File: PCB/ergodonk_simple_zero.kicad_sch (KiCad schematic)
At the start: 147 parts, among them J2 4PIN, Q1 TIP120, SW0 SW_PUSH_LED, SW08 SW_PUSH_LED, SW1 SW_PUSH_LED, SW10 SW_PUSH_LED, SW11 SW_PUSH_LED, SW12 SW_PUSH_LED, SW13 SW_PUSH_LED, SW14 SW_PUSH_LED, SW15 SW_PUSH_LED, SW16 SW_PUSH_LED, SW17 SW_PUSH_LED, SW18 SW_PUSH_LED, SW2 SW_PUSH_LED, SW20 SW_PUSH_LED, SW21 SW_PUSH_LED, SW22 SW_PUSH_LED, SW23 SW_PUSH_LED, SW24 SW_PUSH_LED, SW25 SW_PUSH_LED, SW26 SW_PUSH_LED, SW27 SW_PUSH_LED, SW28 SW_PUSH_LED, SW3 SW_PUSH_LED, SW30 SW_PUSH_LED, SW31 SW_PUSH_LED, SW32 SW_PUSH_LED, SW33 SW_PUSH_LED, SW34 SW_PUSH_LED, SW35 SW_PUSH_LED, SW36 SW_PUSH_LED, SW37 SW_PUSH_LED, SW38 SW_PUSH_LED, SW4 SW_PUSH_LED, SW40 SW_PUSH_LED, SW42 SW_PUSH_LED, SW43 SW_PUSH_LED, SW44 SW_PUSH_LED, SW45 SW_PUSH_LED, SW46 SW_PUSH_LED, SW47 SW_PUSH_LED, SW48 SW_PUSH_LED, SW5 SW_PUSH_LED, SW50 SW_PUSH_LED, SW51 SW_PUSH_LED, SW52 SW_PUSH_LED, SW53 SW_PUSH_LED, SW54 SW_PUSH_LED, SW55 SW_PUSH_LED, SW56 SW_PUSH_LED, SW57 SW_PUSH_LED, SW58 SW_PUSH_LED, SW6 SW_PUSH_LED, SW7 SW_PUSH_LED

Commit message: Fixed key plate hole width bug Updated home position for keyplate footprints Generated bottom plate for acrylic production
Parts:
- H20, H24, H4: footprint Ergodonk_simple_zero:Hole from sofle for M2 posts gold rimmer -> Ergodonk_simple_zero:M2 Standoff hole - keyplate passthrough
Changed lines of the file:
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@@
       (effects (font (size 1.27 1.27)) (justify left))
     )
-    (property "Footprint" "Ergodonk_simple_zero:Hole from sofle for M2 posts gold rimmer" (at 273.05 229.87 0)
+    (property "Footprint" "Ergodonk_simple_zero:M2 Standoff hole - keyplate passthrough" (at 273.05 229.87 0)
       (effects (font (size 1.27 1.27)) hide)
     )
@@
       (effects (font (size 1.27 1.27)) (justify left))
     )
-    (property "Footprint" "Ergodonk_simple_zero:Hole from sofle for M2 posts gold rimmer" (at 223.52 229.87 0)
+    (property "Footprint" "Ergodonk_simple_zero:M2 Standoff hole - keyplate passthrough" (at 223.52 229.87 0)
       (effects (font (size 1.27 1.27)) hide)
     )
@@
       (effects (font (size 1.27 1.27)) (justify left))
     )
-    (property "Footprint" "Ergodonk_simple_zero:Hole from sofle for M2 posts gold rimmer" (at 251.46 260.35 0)
-      (effects (font (size 1.27 1.27)) hide)
-    )
+    (property "Footprint" "Ergodonk_simple_zero:M2 Standoff hole - keyplate passthrough" (at 251.46 260.35 0)
+      (effects (font (size 1.27 1.27)) hide)
+    )

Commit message: Fixed switched thumb keys for SA labels
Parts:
- SW51: LH + -> 0
- SW52: LH 0 -> +
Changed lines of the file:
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@@
       (effects (font (size 1.27 1.27)) hide)
     )
-    (property "LH" "0" (at 364.49 149.86 0) (show_name)
+    (property "LH" "+" (at 364.49 149.86 0) (show_name)
       (effects (font (size 1.27 1.27)))
     )
@@
       (effects (font (size 1.27 1.27)) hide)
     )
-    (property "LH" "+" (at 386.08 149.86 0) (show_name)
-      (effects (font (size 1.27 1.27)))
-    )
+    (property "LH" "0" (at 386.08 149.86 0) (show_name)
+      (effects (font (size 1.27 1.27)))
+    )

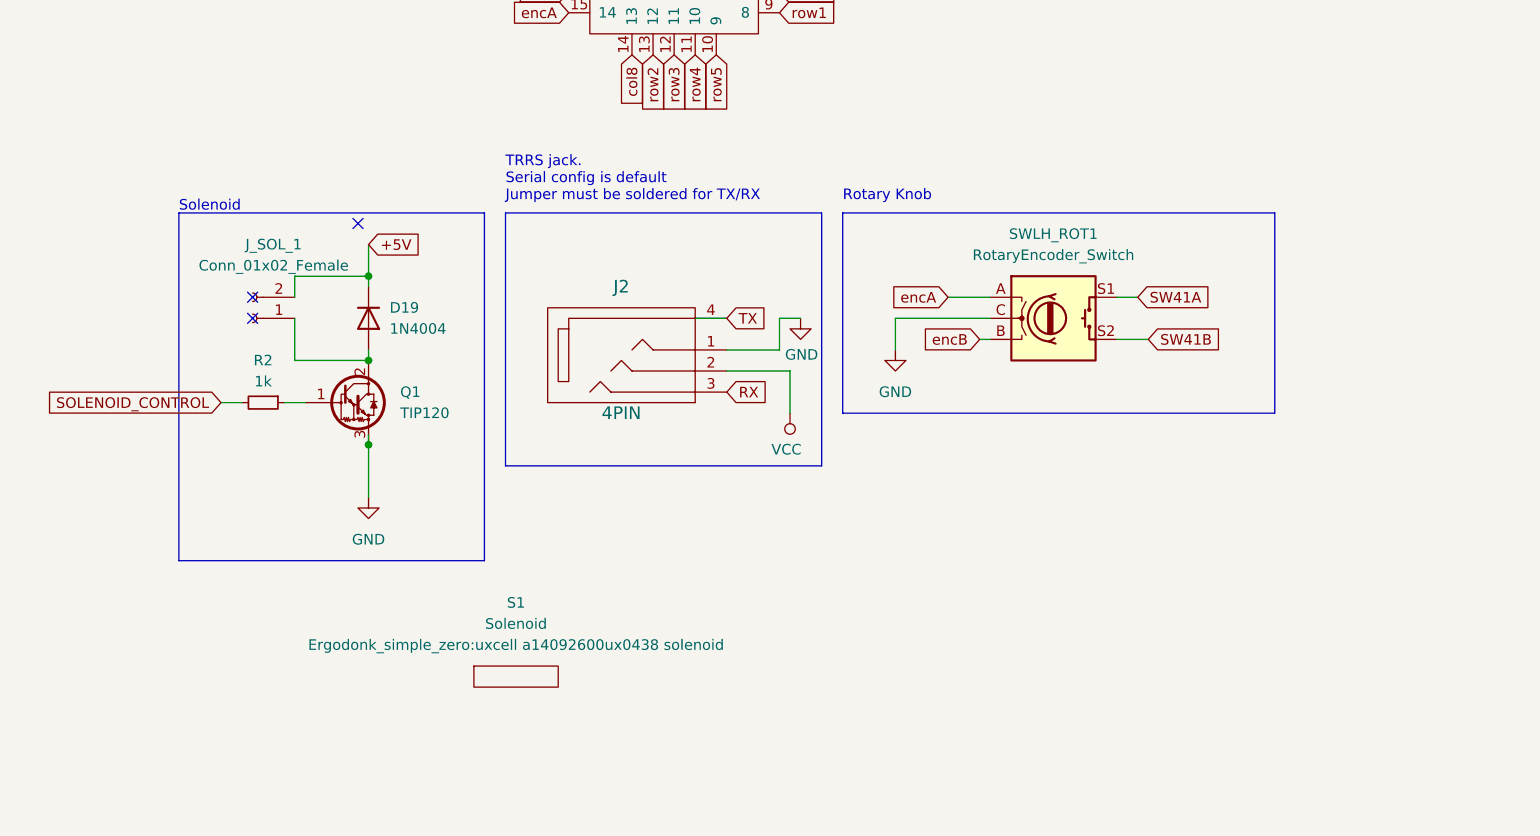
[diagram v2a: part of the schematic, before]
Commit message: Added alternate solenoid connection point
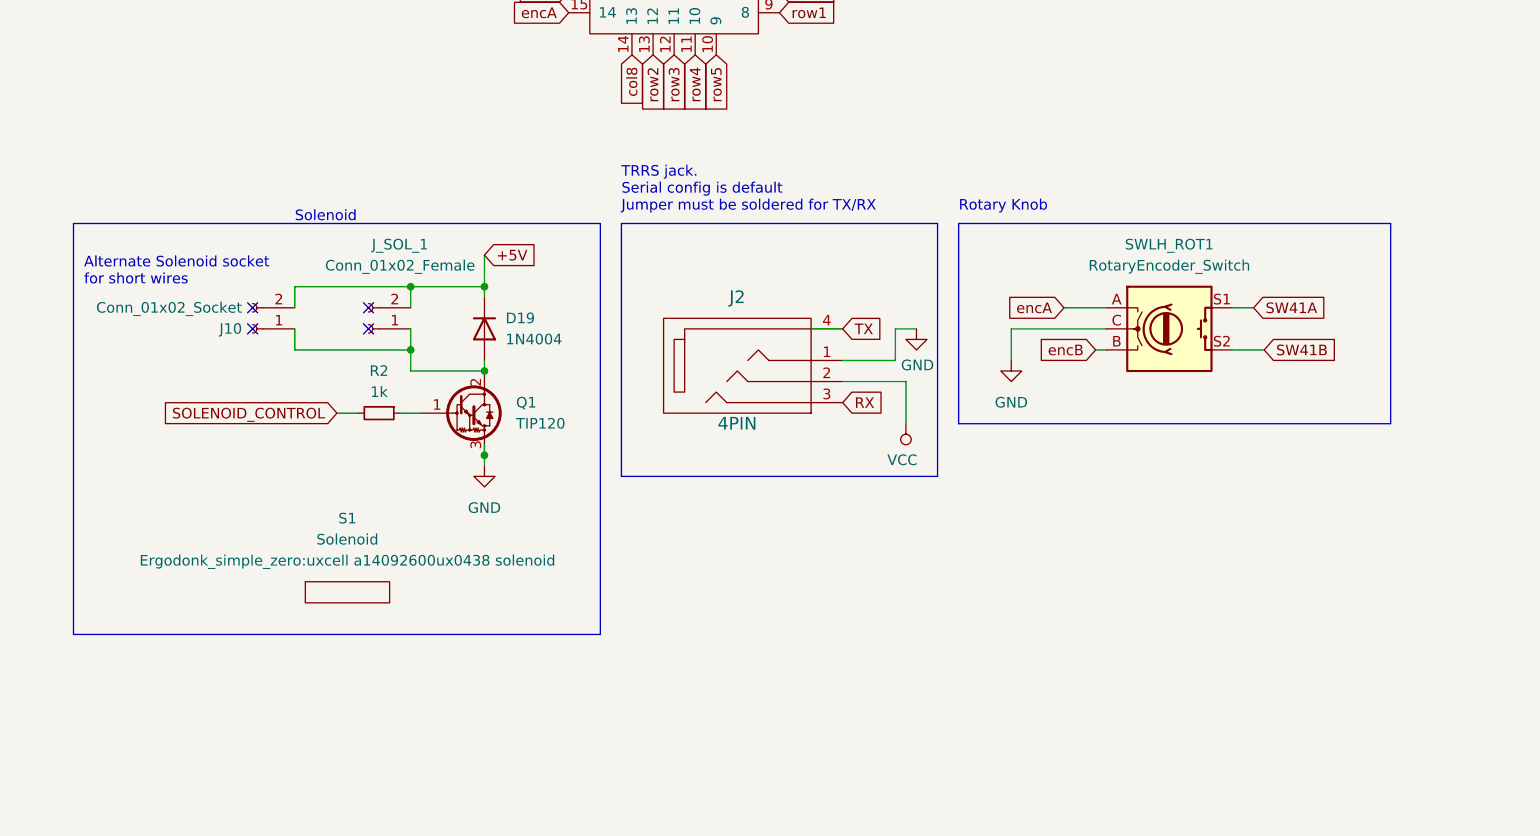
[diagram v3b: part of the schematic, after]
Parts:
- added J10: Conn_01x02_Socket, Ergodonk_simple_zero:PinHeader_1x02_P2.54mm_Vertical, symbol Connector:Conn_01x02_Socket
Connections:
- net +5V: now also J10.2 (Pin_2)
- net at D19.2 (A), J_SOL_1.1 (Pin_1), Q1.2 (C): now also J10.1 (Pin_1)
- no-connect marks 3 -> 4
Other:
- note added: "Alternate Solenoid socket for short wires"
- moved on the sheet: D19, J2, J_SOL_1, Q1, R2, S1, SWLH_ROT1
